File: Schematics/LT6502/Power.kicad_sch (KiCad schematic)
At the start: 87 parts, among them IC2 MP2636GR-P, J2 USBPD_PROG, J3 USB_C_Receptacle_USB2.0_16P, J4 BATTERY JST PH-2A, Q1 STL9P3LLH6, Q3 STL9P3LLH6, U6 STUSB4500QTR, U7 AP63203WU

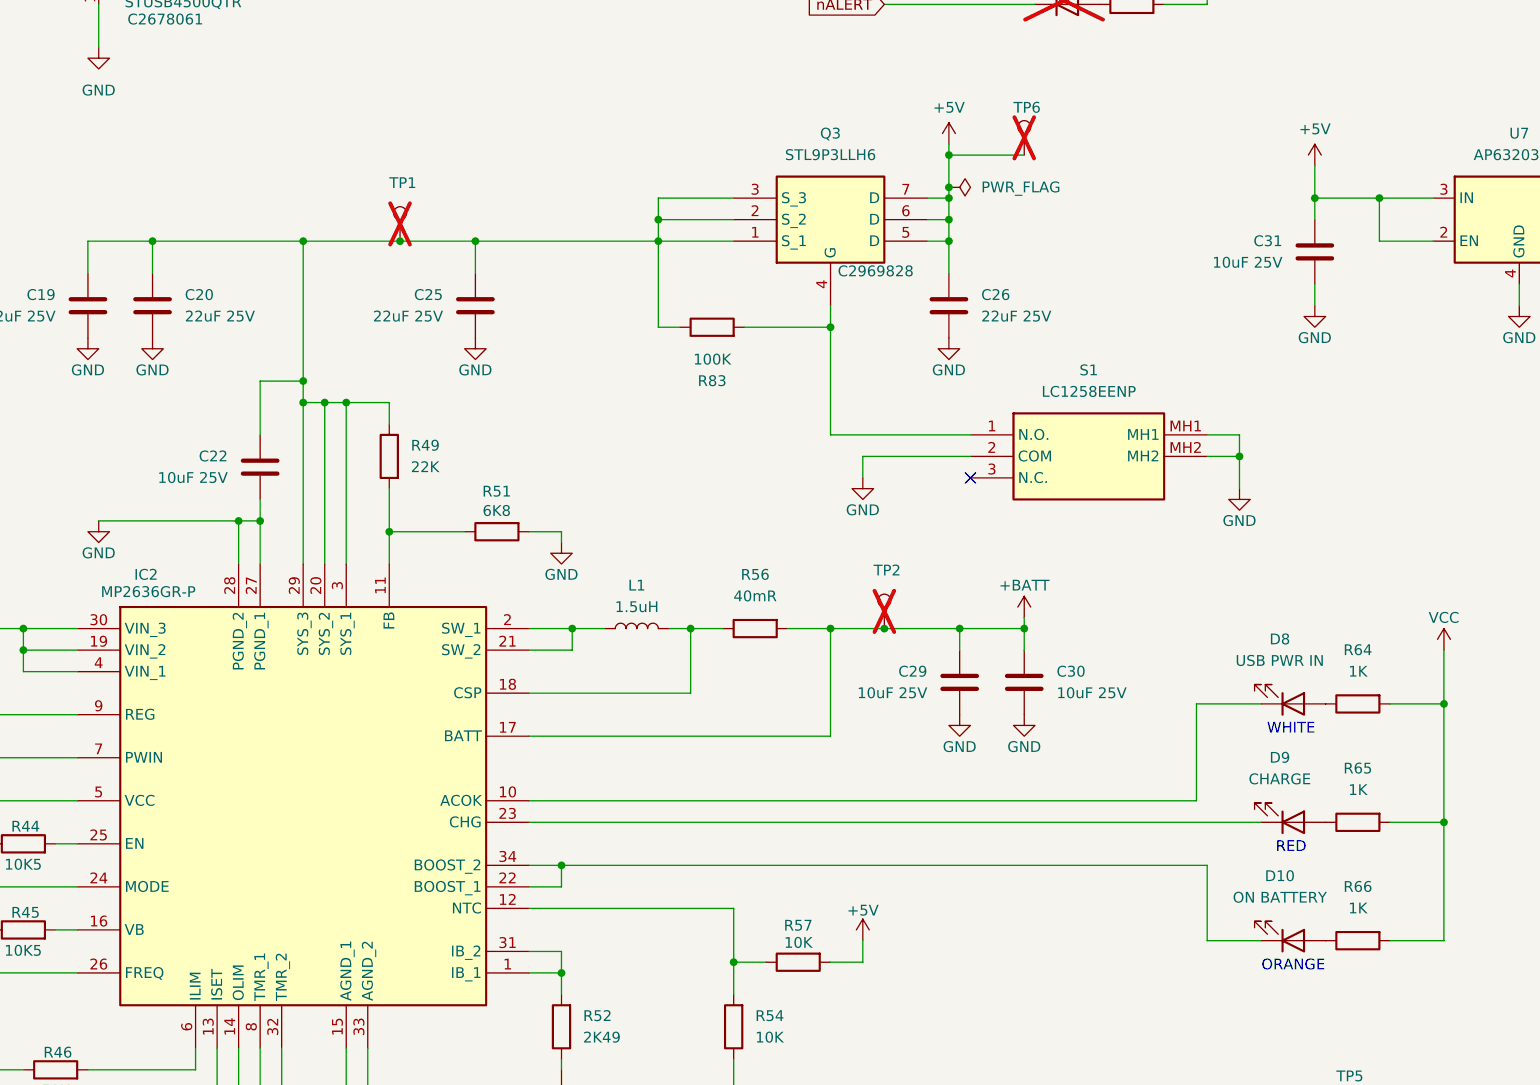
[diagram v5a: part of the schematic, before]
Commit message: Expansion Template + Main Board update
Created an expansion board template with main connector and correct PCB size
Fixed bug with Charging circuit on main board that meant it wouldn't charge when off.
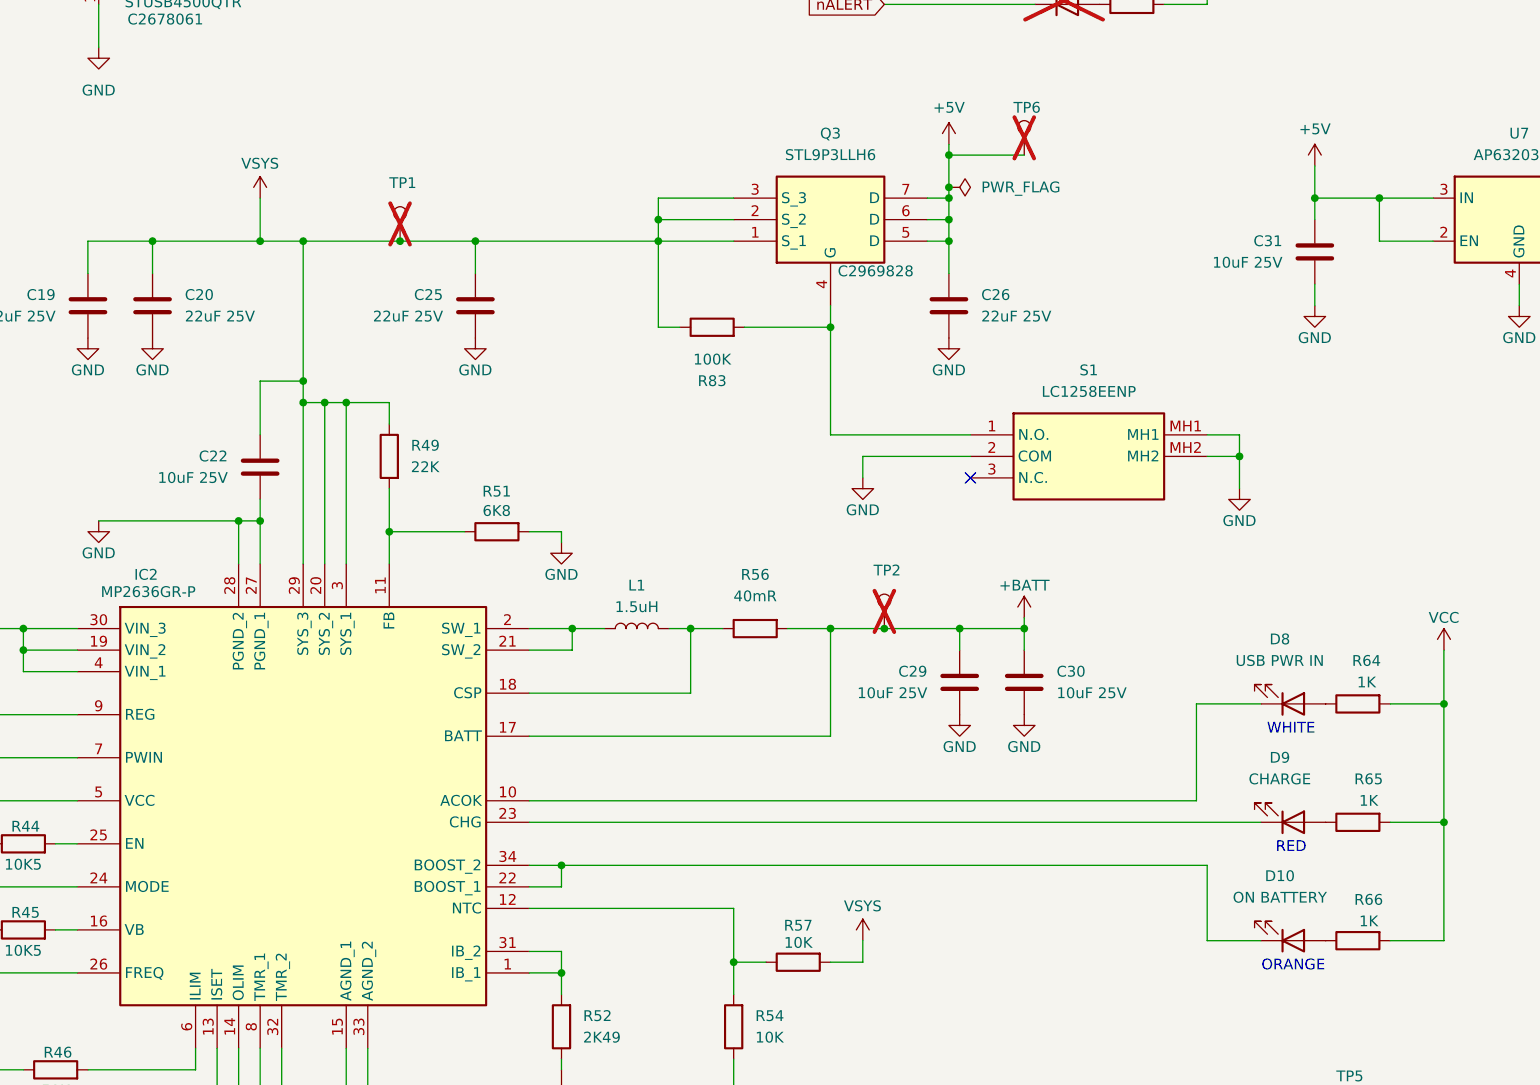
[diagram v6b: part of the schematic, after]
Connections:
- net +5V: no longer R57.2
- net VSYS: now reaches C19.1, C20.1, C22.1, C25.1, IC2.20 (SYS_2), IC2.29 (SYS_3), IC2.3 (SYS_1), Q3.1 (S_1), Q3.2 (S_2), Q3.3 (S_3), R49.1, R83.1, TP1.1
- net VSYS: now also R57.2
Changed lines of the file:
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@@
 	)
 	(junction
+		(at 184.15 133.35)
+		(diameter 0)
+		(color 0 0 0 0)
+	)
+	(junction
 		(at 200.66 133.35)
 		(diameter 0)
@@
 	(wire
 		(pts
-			(xy 171.45 133.35) (xy 189.23 133.35)
+			(xy 171.45 133.35) (xy 184.15 133.35)
 		)
 		(stroke
@@
 	(wire
 		(pts
+			(xy 184.15 128.27) (xy 184.15 133.35)
+		)
+		(stroke
+			(width 0)
+			(type default)
+		)
+	)
+	(wire
+		(pts
 			(xy 163.83 137.16) (xy 163.83 133.35)
 		)
@@
 	(wire
 		(pts
+			(xy 184.15 133.35) (xy 189.23 133.35)
+		)
+		(stroke
+			(width 0)
+			(type default)
+		)
+	)
+	(wire
+		(pts
 			(xy 303.53 26.67) (xy 307.34 26.67)
 		)
@@
 		(on_board yes)
 		(dnp no)
-		(fields_autoplaced yes)
 		(property "Reference" "R66"
-			(at 313.69 209.55 90)
+			(at 314.96 211.074 90)
 			(effects
 				(font
@@
 		)
 		(property "Value" "1K"
-			(at 313.69 212.09 90)
+			(at 314.96 213.614 90)
 			(effects
 				(font
@@
 	)
 	(symbol
+		(lib_id "power:VPP")
+		(at 255.27 215.9 0)
+		(unit 1)
+		(exclude_from_sim no)
+		(in_bom yes)
+		(on_board yes)
+		(dnp no)
+		(property "Reference" "#PWR0120"
+			(at 255.27 219.71 0)
+			(effects
+				(font
+					(size 1.27 1.27)
+				)
+				(hide yes)
+			)
+		)
+		(property "Value" "VSYS"
+			(at 255.27 211.836 0)
+			(effects
+				(font
+					(size 1.27 1.27)
+				)
+			)
+		)
+		(property "Footprint" ""
+			(at 255.27 215.9 0)
+			(effects
+				(font
+					(size 1.27 1.27)
+				)
+				(hide yes)
+			)
+		)
+		(property "Datasheet" ""
+			(at 255.27 215.9 0)
+			(effects
+				(font
+					(size 1.27 1.27)
+				)
+				(hide yes)
+			)
+		)
+		(property "Description" "Power symbol creates a global label with name \"VPP\""
+			(at 255.27 215.9 0)
+			(effects
+				(font
+					(size 1.27 1.27)
+				)
+				(hide yes)
+			)
+		)
+		(pin "1"
+		)
+		(instances
+			(project "LT6502"
+				(path "/a2243a34-697c-4939-97f7-df548e421864/023ed7d3-fbe9-4017-a116-821cc1971589"
+					(reference "#PWR0120")
+					(unit 1)
+				)
+			)
+		)
+	)
+	(symbol
 		(lib_id "power:VCC")
 		(at 137.16 199.39 0)
@@
 		(on_board yes)
 		(dnp no)
-		(fields_autoplaced yes)
 		(property "Reference" "R64"
-			(at 313.69 181.61 90)
+			(at 314.706 182.88 90)
 			(effects
 				(font
@@
 		)
 		(property "Value" "1K"
-			(at 313.69 184.15 90)
+			(at 314.706 185.42 90)
 			(effects
 				(font
@@
 	)
 	(symbol
+		(lib_id "power:VPP")
+		(at 184.15 128.27 0)
+		(unit 1)
+		(exclude_from_sim no)
+		(in_bom yes)
+		(on_board yes)
+		(dnp no)
+		(property "Reference" "#PWR0147"
+			(at 184.15 132.08 0)
+			(effects
+				(font
+					(size 1.27 1.27)
+				)
+				(hide yes)
+			)
+		)
+		(property "Value" "VSYS"
+			(at 184.15 124.206 0)
+			(effects
+				(font
+					(size 1.27 1.27)
+				)
+			)
+		)
+		(property "Footprint" ""
+			(at 184.15 128.27 0)
+			(effects
+				(font
+					(size 1.27 1.27)
+				)
+				(hide yes)
+			)
+		)
+		(property "Datasheet" ""
+			(at 184.15 128.27 0)
+			(effects
+				(font
+					(size 1.27 1.27)
+				)
+				(hide yes)
+			)
+		)
+		(property "Description" "Power symbol creates a global label with name \"VPP\""
+			(at 184.15 128.27 0)
+			(effects
+				(font
+					(size 1.27 1.27)
+				)
+				(hide yes)
+			)
+		)
+		(pin "1"
+		)
+		(instances
+			(project ""
+				(path "/a2243a34-697c-4939-97f7-df548e421864/023ed7d3-fbe9-4017-a116-821cc1971589"
+					(reference "#PWR0147")
+					(unit 1)
+				)
+			)
+		)
+	)
+	(symbol
 		(lib_id "Device:R")
 		(at 287.02 92.71 90)
@@
 	)
 	(symbol
-		(lib_id "power:+5V")
-		(at 255.27 215.9 0)
-		(unit 1)
-		(exclude_from_sim no)
-		(in_bom yes)
-		(on_board yes)
-		(dnp no)
-		(property "Reference" "#PWR0120"
-			(at 255.27 219.71 0)
-			(effects
-				(font
-					(size 1.27 1.27)
-				)
-				(hide yes)
-			)
-		)
-		(property "Value" "+5V"
-			(at 255.27 212.344 0)
-			(effects
-				(font
-					(size 1.27 1.27)
-				)
-			)
-		)
-		(property "Footprint" ""
-			(at 255.27 215.9 0)
-			(effects
-				(font
-					(size 1.27 1.27)
-				)
-				(hide yes)
-			)
-		)
-		(property "Datasheet" ""
-			(at 255.27 215.9 0)
-			(effects
-				(font
-					(size 1.27 1.27)
-				)
-				(hide yes)
-			)
-		)
-		(property "Description" "Power symbol creates a global label with name \"+5V\""
-			(at 255.27 215.9 0)
-			(effects
-				(font
-					(size 1.27 1.27)
-				)
-				(hide yes)
-			)
-		)
-		(pin "1"
-		)
-		(instances
-			(project "LT6502"
-				(path "/a2243a34-697c-4939-97f7-df548e421864/023ed7d3-fbe9-4017-a116-821cc1971589"
-					(reference "#PWR0120")
-					(unit 1)
-				)
-			)
-		)
-	)
-	(symbol
 		(lib_id "Device:C")
 		(at 102.87 185.42 0)
@@
 		(on_board yes)
 		(dnp no)
-		(fields_autoplaced yes)
 		(property "Reference" "R65"
-			(at 313.69 195.58 90)
+			(at 314.96 196.85 90)
 			(effects
 				(font
@@
 		)
 		(property "Value" "1K"
-			(at 313.69 198.12 90)
+			(at 314.96 199.39 90)
 			(effects
 				(font

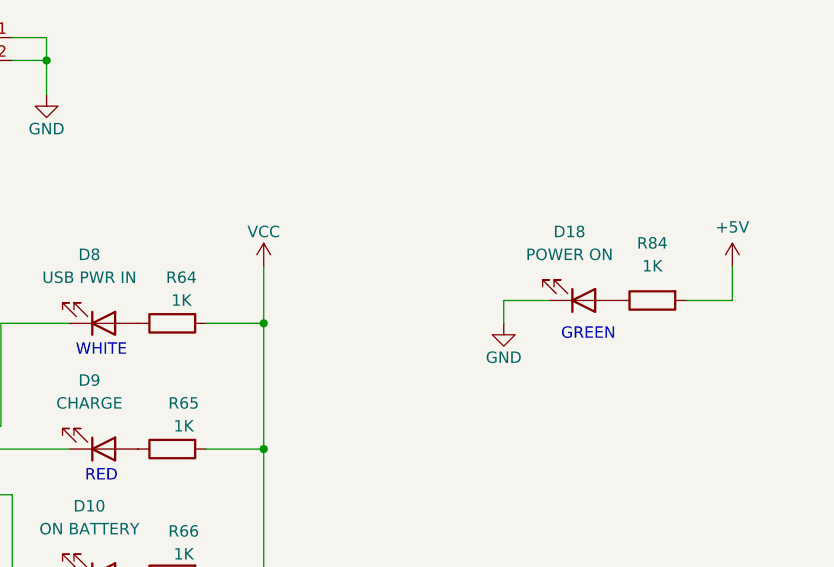
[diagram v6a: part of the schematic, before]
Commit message: LED value change, added fix for FTDI power
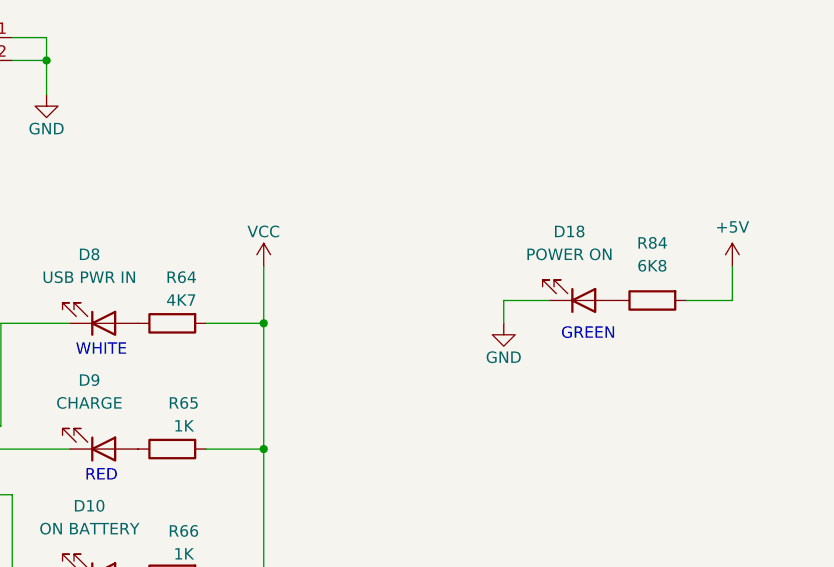
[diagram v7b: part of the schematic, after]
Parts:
- R64: value 1K -> 4K7; LCSC C11702 -> (none)
- R84: value 1K -> 6K8; LCSC C11702 -> (none)
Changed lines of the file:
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@@
 			)
 		)
-		(property "Value" "1K"
+		(property "Value" "6K8"
 			(at 367.03 181.61 90)
 			(effects
@@
 			)
 		)
-		(property "LCSC" "C11702"
+		(property "LCSC" ""
 			(at 367.03 185.42 90)
 			(effects
@@
 			)
 		)
-		(property "Value" "1K"
+		(property "Value" "4K7"
 			(at 314.706 185.42 90)
 			(effects
@@
 			)
 		)
-		(property "LCSC" "C11702"
+		(property "LCSC" ""
 			(at 313.69 187.96 90)
 			(effects

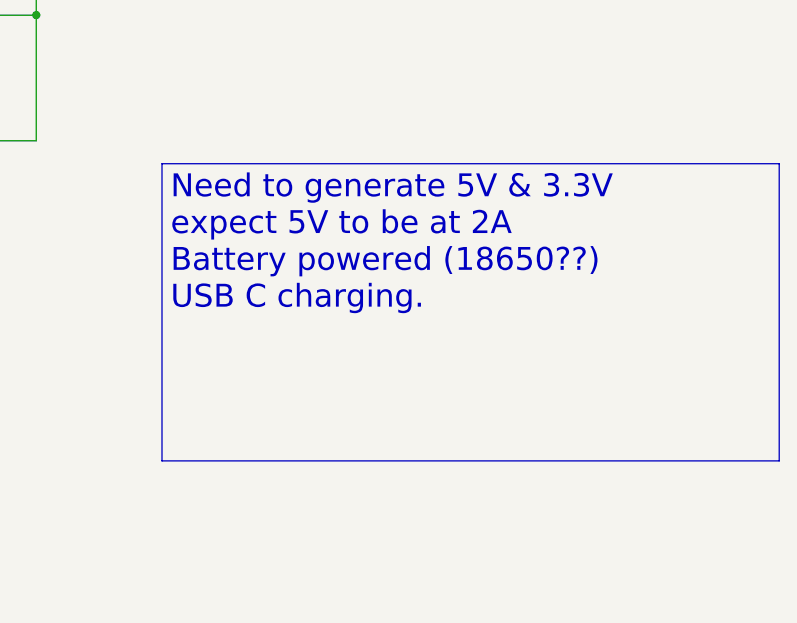
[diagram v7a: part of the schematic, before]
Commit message: PCB/Schematic edits
moved speaker hole a little
made nRES resistor for display no fit (this upsets them for some reason)
Added diodes to ensure USB Console chip is powered when nothing attached (this causes issues with booting.
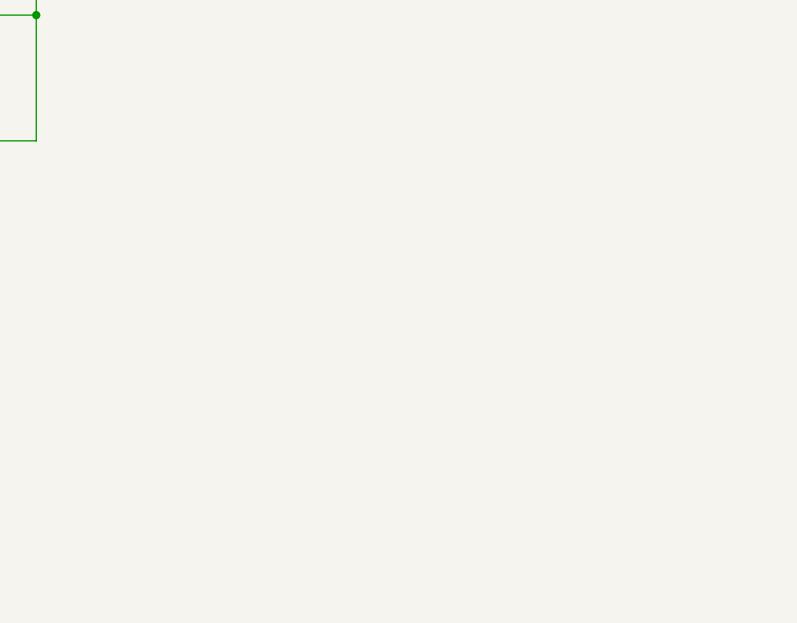
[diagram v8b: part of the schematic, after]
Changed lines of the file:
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@@
-		)
-	)
-	(text_box "Need to generate 5V & 3.3V\nexpect 5V to be at 2A\nBattery powered (18650??) \nUSB C charging."
-		(exclude_from_sim no)
-		(at 337.82 218.44 0)
-		(size 68.58 33.02)
-		(margins 0.9525 0.9525 0.9525 0.9525)
-		(stroke
-			(width 0)
-			(type solid)
-		)
-		(fill
-			(type none)
-		)
-		(effects
-			(font
-				(size 2.54 2.54)
-			)
-			(justify left top)
 		)
 	)
